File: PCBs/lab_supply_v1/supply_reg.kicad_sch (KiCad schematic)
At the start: 43 parts, among them Q1 Q_NPN_BEC, Q2 Q_NPN_BEC, U10 LM334Z, U11 NCS20071SN2T1G, U3 LT3080xMS8E, U4 LT3080xMS8E, U5 LT3080xMS8E, U6 LT3080xMS8E, U7 LT3080xMS8E, U8 LT6106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

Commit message: Updated PCB, FTDI interface
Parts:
- removed L4: 3.3uH, symbol Device:L
- added FB2: Ferrite_Bead, symbol PCM_Device_AKL:Ferrite_Bead
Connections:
- net +32V: now also FB2.1
- net at C17.1, R13.1, U8.4 (+): now also FB2.2
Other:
- note added: "output current: ~3.17 mA"
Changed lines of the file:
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@@
+		)
+	)
+	(text "output current: ~3.17 mA"
+		(exclude_from_sim no)
+		(at 84.328 99.822 0)
+		(effects
+			(font
+				(size 1.27 1.27)
+			)
 		)
 	)
@@
 	)
 	(symbol
-		(lib_id "Device:L")
-		(at 30.48 26.67 90)
-		(unit 1)
-		(exclude_from_sim no)
-		(in_bom yes)
-		(on_board yes)
-		(dnp no)
-		(fields_autoplaced yes)
-		(property "Reference" "L4"
-			(at 30.48 21.59 90)
-			(effects
-				(font
-					(size 1.27 1.27)
-				)
-			)
-		)
-		(property "Value" "3.3uH"
-			(at 30.48 24.13 90)
-			(effects
-				(font
-					(size 1.27 1.27)
-				)
-			)
-		)
-		(property "Footprint" ""
-			(at 30.48 26.67 0)
-			(effects
-				(font
-					(size 1.27 1.27)
-				)
-				(hide yes)
-			)
-		)
-		(property "Datasheet" "~"
-			(at 30.48 26.67 0)
-			(effects
-				(font
-					(size 1.27 1.27)
-				)
-				(hide yes)
-			)
-		)
-		(property "Description" "Inductor"
-			(at 30.48 26.67 0)
-			(effects
-				(font
-					(size 1.27 1.27)
-				)
-				(hide yes)
-			)
-		)
-		(pin "2"
-		)
-		(pin "1"
-		)
-		(instances
-			(project "lab_supply_v1"
-				(path "/c381ddef-a21e-4847-9921-7e6cff5e49a3/d7d64f56-cfcf-4597-a335-fa2fd63e09bc"
-					(reference "L4")
-					(unit 1)
-				)
-			)
-		)
-	)
-	(symbol
 		(lib_id "Device:R_Small")
 		(at 153.67 71.12 90)
@@
 					(unit 1)
 				)
+			)
+		)
+	)
+	(symbol
+		(lib_id "PCM_Device_AKL:Ferrite_Bead")
+		(at 30.48 26.67 0)
+		(unit 1)
+		(exclude_from_sim no)
+		(in_bom yes)
+		(on_board yes)
+		(dnp no)
+		(property "Reference" "FB2"
+			(at 30.226 24.13 0)
+			(effects
+				(font
+					(size 1.27 1.27)
+				)
+			)
+		)
+		(property "Value" "Ferrite_Bead"
+			(at 30.48 22.86 0)
+			(effects
+				(font
+					(size 1.27 1.27)
+				)
+				(hide yes)
+			)
+		)
+		(property "Footprint" ""
+			(at 30.48 23.368 0)
+			(effects
+				(font
+					(size 1.27 1.27)
+				)
+				(hide yes)
+			)
+		)
+		(property "Datasheet" "~"
+			(at 30.48 26.67 90)
+			(effects
+				(font
+					(size 1.27 1.27)
+				)
+				(hide yes)
+			)
+		)
+		(property "Description" "Ferrite bead, Alternate KiCAD Library"
+			(at 30.48 26.67 0)
+			(effects
+				(font
+					(size 1.27 1.27)
+				)
+				(hide yes)
+			)
+		)
+		(pin "2"
+		)
+		(pin "1"
+		)
+		(instances
+			(project "lab_supply_v1"
+				(path "/c381ddef-a21e-4847-9921-7e6cff5e49a3/d7d64f56-cfcf-4597-a335-fa2fd63e09bc"
+					(reference "FB2")
+					(unit 1)
+				)

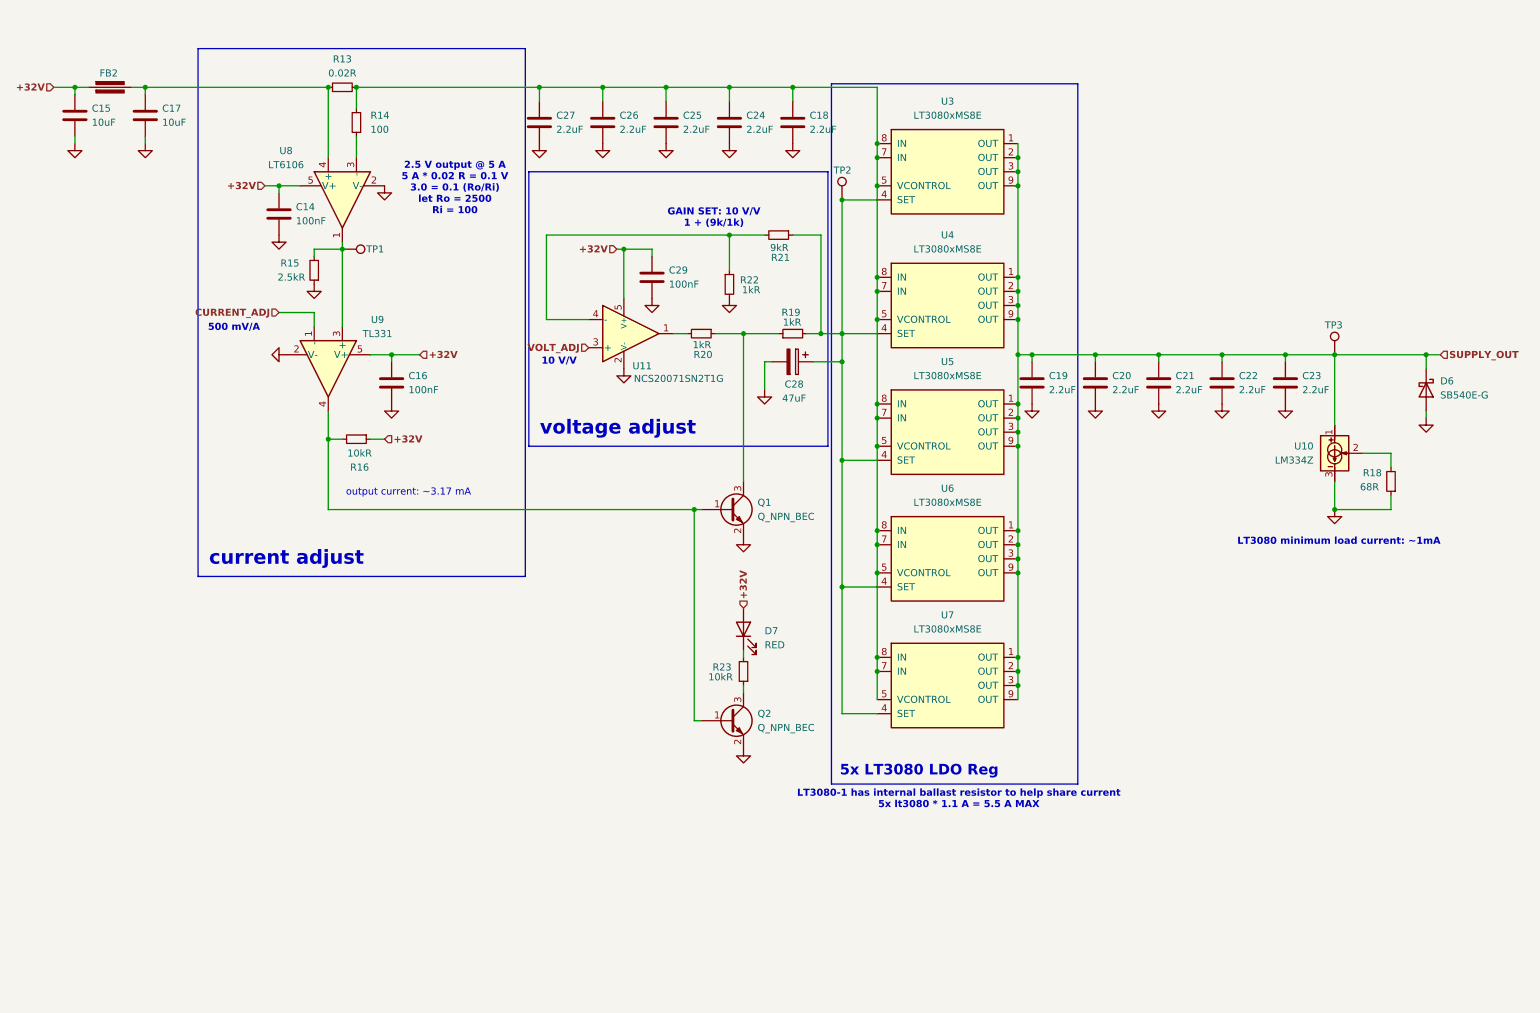
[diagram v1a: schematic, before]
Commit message: PCB updated, voltage/current sensing
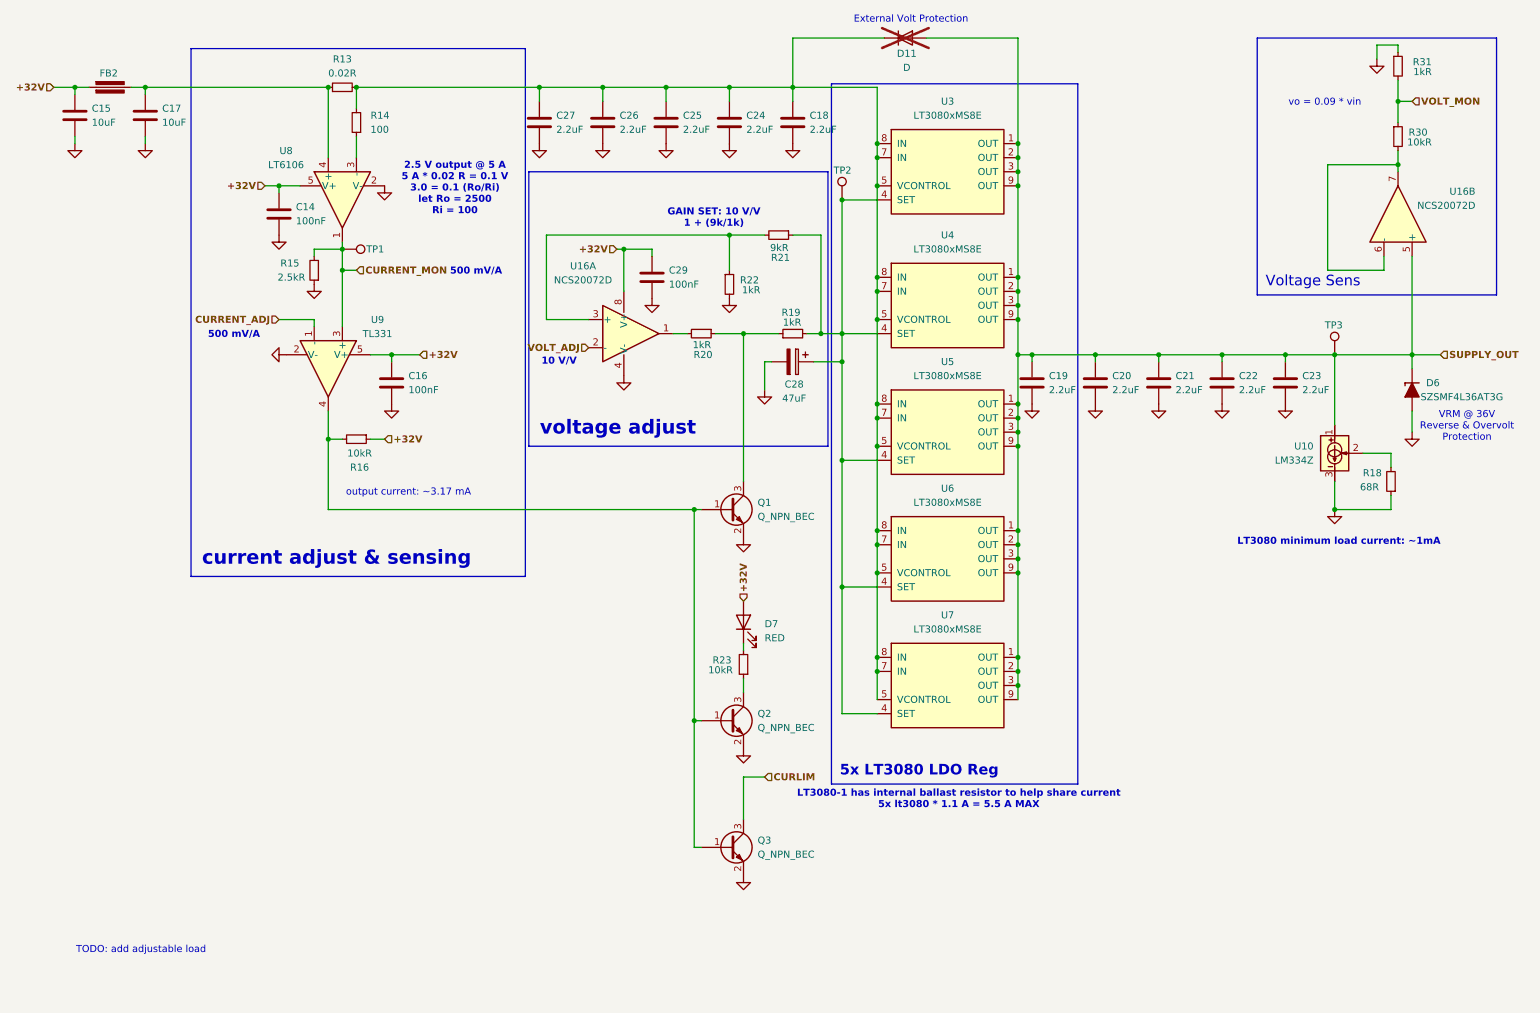
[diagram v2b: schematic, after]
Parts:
- removed D6: SB540E-G, symbol Device:D_Schottky
- removed U11: NCS20071SN2T1G, Package_SO_AKL:TSOP-5_1.65x3.05mm_P0.95mm, symbol PCM_Amplifier_Operational_AKL:NCS20071SN2T1G
- added D11: D, symbol Device:D
- added D6: SZSMF4L36AT3G, symbol PCM_Diode_TVS_AKL:D_TVS_Unidirectional_Generic
- added Q3: Q_NPN_BEC, symbol Device:Q_NPN_BEC
- added R30: 10kR, symbol Device:R_Small
- added R31: 1kR, symbol Device:R_Small
- added U16: NCS20072D, Package_SO:SOIC-8_3.9x4.9mm_P1.27mm, symbol Amplifier_Operational:NCS20072D
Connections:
- net +32V: now also U16.8 (V+)
- net GND: now also D6.2 (A), Q3.2 (E), R31.1, U16.4 (V-)
- net SUPPLY_OUT: now also D11.2 (A), D6.1 (K), U16.5 (+)
- net VOLT_ADJ: now also U16.2 (-)
- net at Q1.1 (B), Q2.1 (B), R16.2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: now also Q3.1 (B)
- net at C18.1, C24.1, C25.1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: now also D11.1 (K)
- net at R21.2, R22.1: now also U16.3 (+)
- net at R20.2: now also U16.1
- net CURRENT_MON: now reaches R15.2, TP1.1, U8.1, U9.3 (+)
- new net: R30.2, U16.6 (-), U16.7
- new net CURLIM: Q3.3 (C)
- new net VOLT_MON: R30.1, R31.2
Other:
- note added: "External Volt Protection"
- note added: "TODO: add adjustable load"
- note added: "VRM @ 36V Reverse & Overvolt Protection"
- note added: "vo = 0.09 * vin"
- moved on the sheet: D7, R23

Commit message: updated current sense values to better suit datasheet requirements
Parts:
- R14: value 100 -> 500R
- R15: value 2.5kR -> 15kR
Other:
- note added: "2.5 V output @ 5 A 5 A * 0.02 R = 0.1 V 3.0 = 0.1 (Ro/Ri) let Ri = 500 Ro = 15k"
- note removed: "2.5 V output @ 5 A 5 A * 0.02 R = 0.1 V 3.0 = 0.1 (Ro/Ri) let Ro = 2500 Ri = 100"
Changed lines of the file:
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@@
 		)
 	)
-	(text "2.5 V output @ 5 A\n5 A * 0.02 R = 0.1 V\n3.0 = 0.1 (Ro/Ri)\nlet Ro = 2500\nRi = 100\n\n"
+	(text "2.5 V output @ 5 A\n5 A * 0.02 R = 0.1 V\n3.0 = 0.1 (Ro/Ri)\nlet Ri = 500\nRo = 15k\n\n"
 		(exclude_from_sim no)
 		(at 92.71 45.974 0)
@@
 			)
 		)
-		(property "Value" "100"
+		(property "Value" "500R"
 			(at 77.47 34.2899 0)
 			(effects
@@
 			)
 		)
-		(property "Value" "2.5kR"
+		(property "Value" "15kR"
 			(at 60.706 60.96 0)
 			(effects

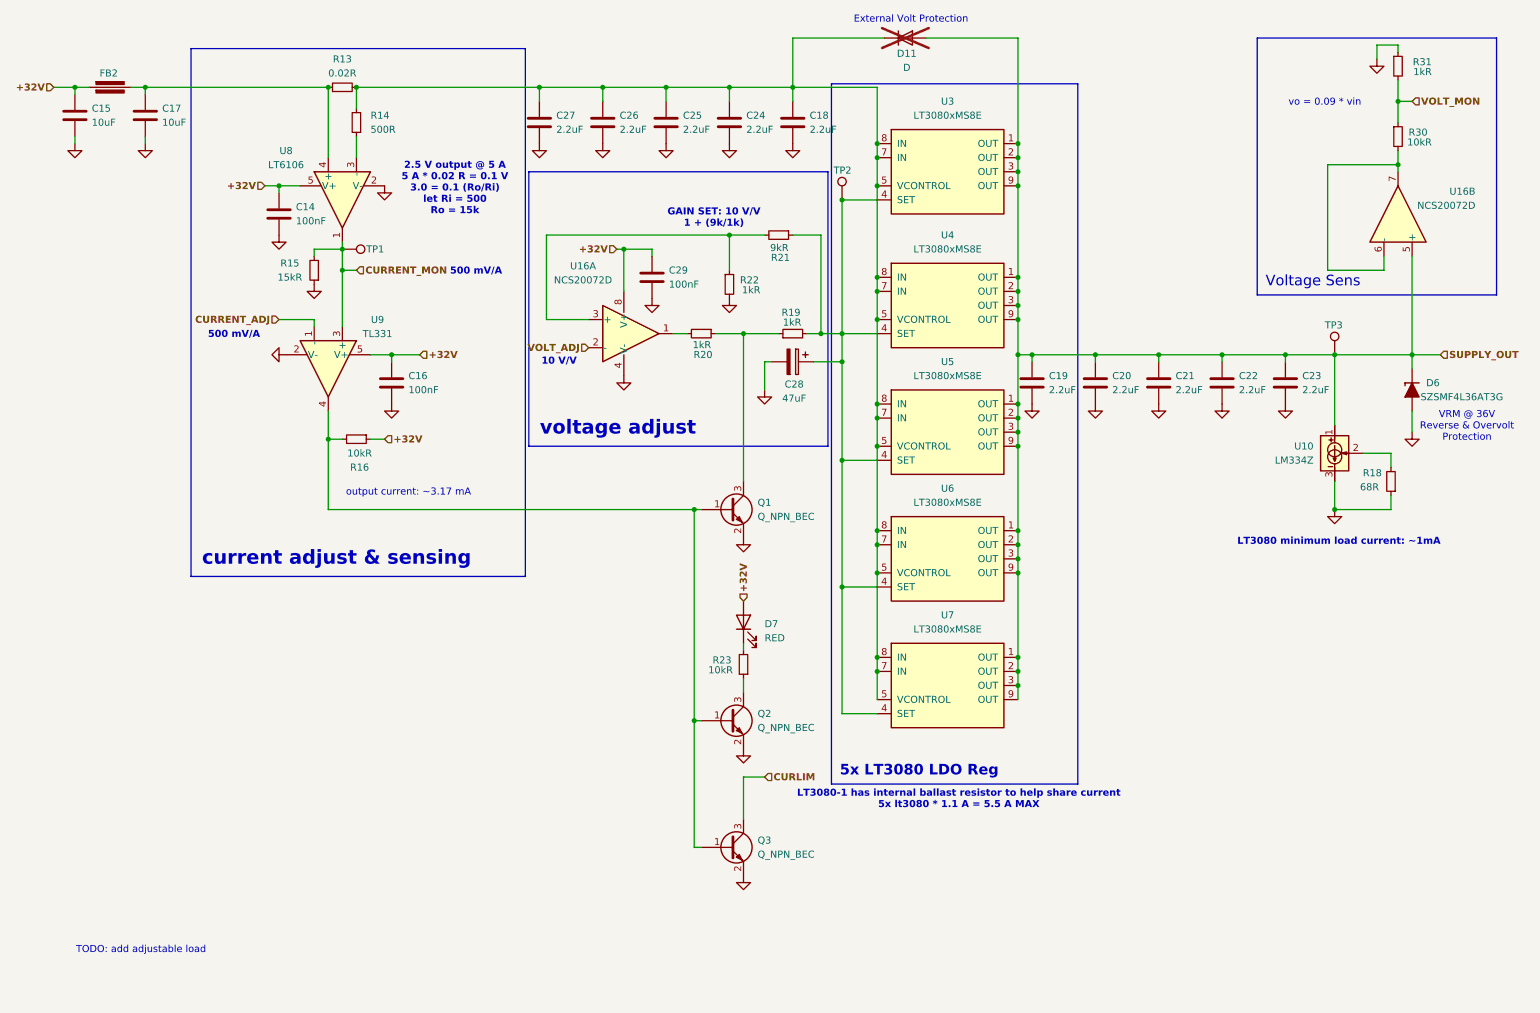
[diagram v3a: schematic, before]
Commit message: Updated PCB Updated feedback circuit for LT3080 SET to reduce BOM Added voltage divider before buffer to help reduce the chance of overvolting V+ pin. Increased values to reduce leakage.
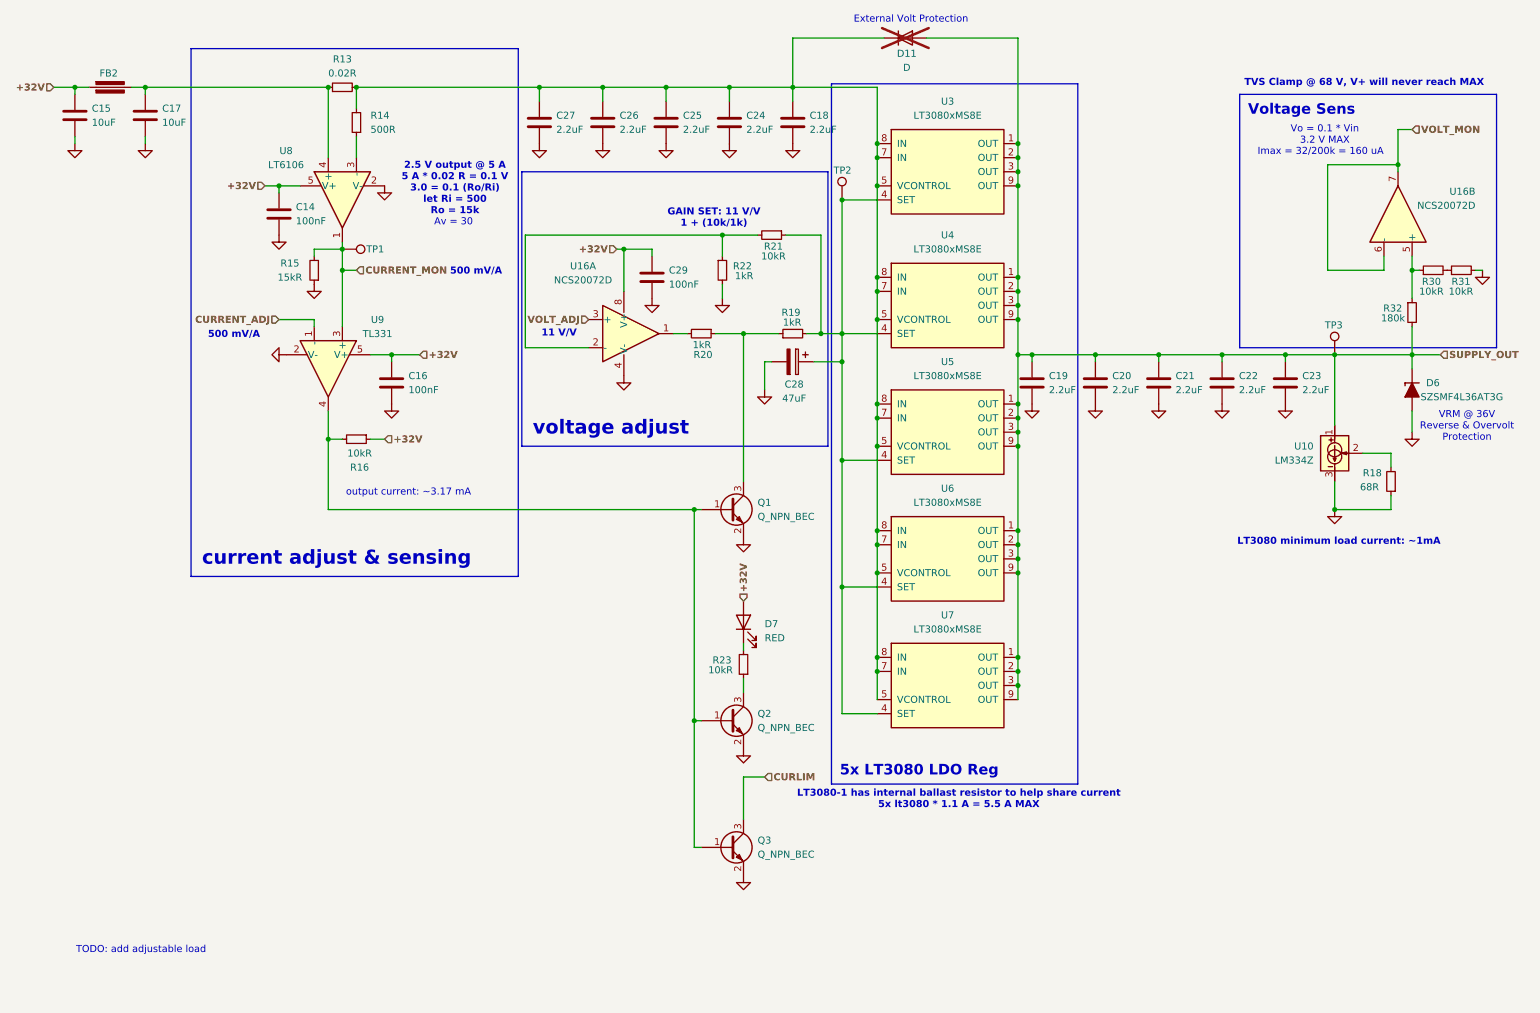
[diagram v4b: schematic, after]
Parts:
- added R32: 180k, symbol Device:R_Small
- R21: value 9kR -> 10kR
- R31: value 1kR -> 10kR
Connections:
- net GND: now also R31.2; no longer R31.1
- net SUPPLY_OUT: now also R32.2; no longer U16.5 (+)
- net VOLT_ADJ: now also U16.3 (+); no longer U16.2 (-)
- net VOLT_MON: now also U16.6 (-), U16.7; no longer R30.1, R31.2
- net at R21.2, R22.1: now also U16.2 (-); no longer U16.3 (+)
- new net: R30.1, R32.1, U16.5 (+)
- new net: R30.2, R31.1
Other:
- note added: "11 V/V"
- note added: "Av = 30"
- note added: "GAIN SET: 11 V/V 1 + (10k/1k)"
- note added: "Imax = 32/200k = 160 uA"
- note added: "TVS Clamp @ 68 V, V+ will never reach MAX"
- note added: "Vo = 0.1 * Vin 3.2 V MAX"
- note removed: "10 V/V"
- note removed: "GAIN SET: 10 V/V 1 + (9k/1k)"
- note removed: "vo = 0.09 * vin"
- moved on the sheet: R22
